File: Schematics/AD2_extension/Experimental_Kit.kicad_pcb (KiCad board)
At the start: 2 copper layers, 69.7 x 76.4 mm, 41 parts, among them J1 I2C, J10 AD2, J11 CN7, J12 CN10, J13 SPI_5V, J2 Keypad, J3 W2, J4 W1, J5 LCD, J6 SPI_3V3, J7 PWM, J8 PWM, J9 AREF, Q1 2N7002, Q2 2N7002, Q3 2N7002, Q4 2N7002, U1 TXU0304PW

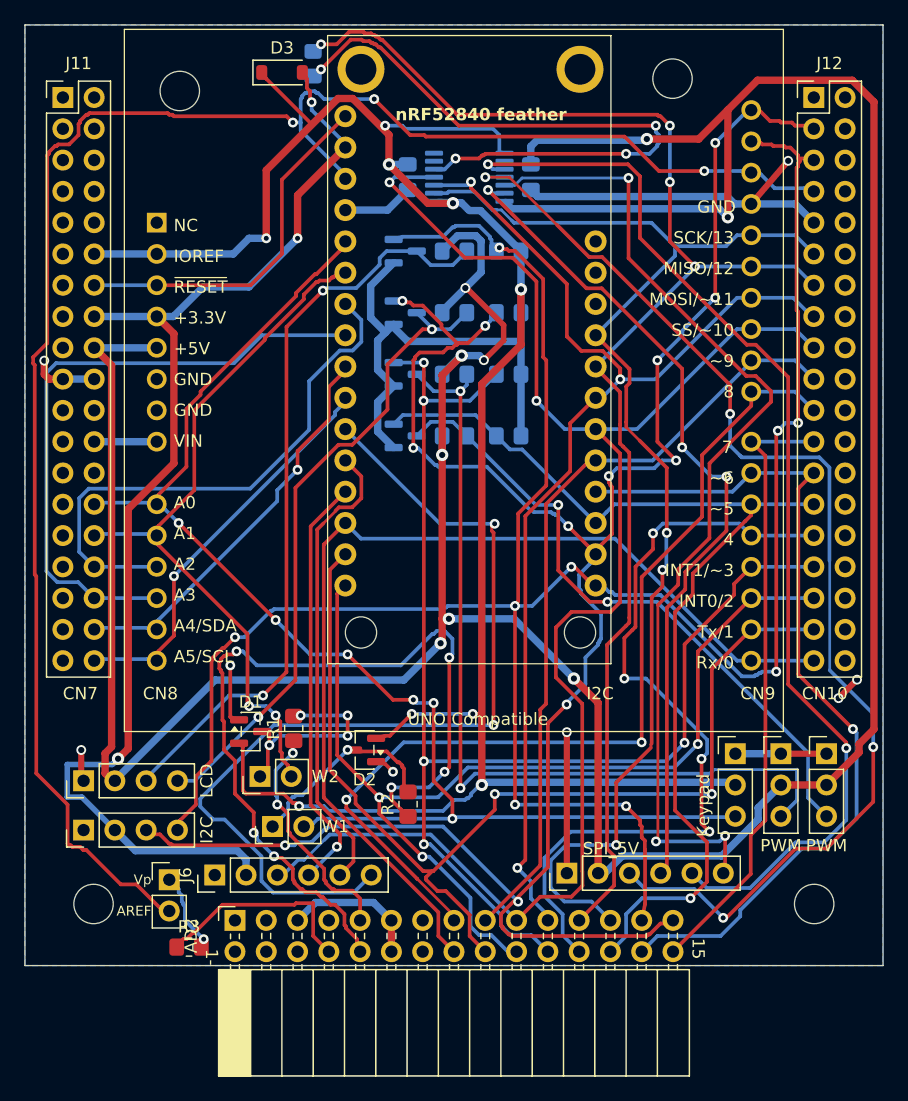
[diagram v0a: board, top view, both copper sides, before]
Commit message: AD2_extension: 보호회로·I2C 버스·Feather 5V 추가, DRC/ERC 무시 항목 0
회로도
- W1/W2 입력 보호: 직렬 1k + BAT54S 클램프, AD2 V+ -> AREF 직렬 4.7k
- IOREF 점퍼를 쇼트키 D3(+3V3 -> IOREF)로 교체
- LCD 시프터와 AD2 I2C를 UNO SDA/SCL, Nucleo PB9/PB8, Feather SDA/SCL 공용 버스로 이전
- U1(TXU0304) OE -> IOREF, MISO 직렬 R13 2.2k
- Feather USB -> D4 -> +5V
- J10/J11/J12 심볼을 필터를 맞춘 프로젝트 사본으로 교체

PCB
- 점퍼 재배치(Nucleo 외곽 밖), W1/W2 정렬, 신규 부품 배치·배선
- 상면 GND 붓기와 스티칭 비아 추가, 배선 직선/45도 정리
- 실크 정리, J10 기판 가장자리용 풋프린트, MS1 코트야드 면제
- ERC/DRC 위반 0, 무시 항목 0

Co-Authored-By: Claude Opus 5.5 <noreply@anthropic.com>
Claude-Session: https://claude.ai/code/session_0124difPG7KsZZNpLXnsU8d2
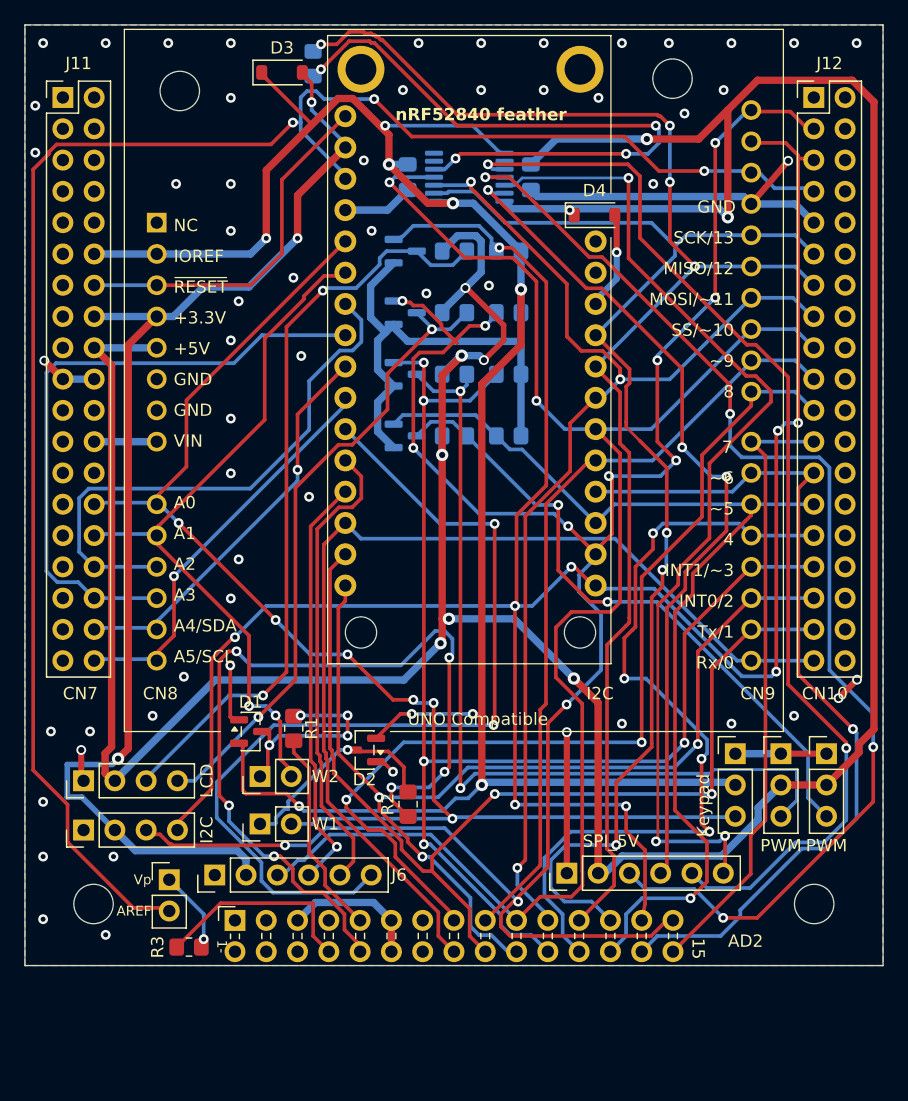
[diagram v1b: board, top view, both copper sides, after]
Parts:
- added D4: 1N5819HW, Diode_SMD:D_SOD-123, F.Cu at (123.2, 59.1)
- J10: footprint Connector_PinSocket_2.54mm:PinSocket_2x15_P2.54mm_Horizontal -> AD2_extension:PinSocket_2x15_P2.54mm_Horizontal_BoardEdge
- moved J4 1.04 mm to (96.0, 108.5)
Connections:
- MS1 pad 26: unconnected-(MS1-USB-Pad26) -> /FEATHER_USB
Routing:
- net /FEATHER_USB: track 0.00 -> 7.87 mm, vias 0 -> 1
- net /W2: track 18.9 -> 16.8 mm, vias 2 -> 0
- net Net-(J6-Pin_6): track 77.3 -> 75.5 mm
- net +3V3: track 99.3 -> 97.6 mm
- net AREF: track 144.1 -> 142.8 mm
- net Net-(D2-K1A2): track 15.9 -> 17.0 mm
- net /A0: track 106.9 -> 107.8 mm
- net /IOREF: track 211.4 -> 210.5 mm
- net /DIO1: track 85.0 -> 84.2 mm
- net GND: track 81.2 -> 80.5 mm, vias 8 -> 58
- net /DIO8: track 76.6 -> 77.3 mm
- net /A5: track 32.7 -> 32.2 mm
- net +5V: track 289.1 -> 289.0 mm, vias 9 -> 10
- added copper zone on F.Cu, net GND
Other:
- board text added: "Dept. of EEC, HKNU 26.10.30"
- board text removed: "Dept. of EEC, HKNU 26.10.09"

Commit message: AD2_extension: 회로도 정리 및 PCB 동기화, README에 이동 경로 추가
- 회로도 정리 반영, PCB 업데이트(FEATHER_USB 넷 → Net-(D4-A))
- ERC 0, DRC 0, 미연결 0, 회로도-PCB 패리티 0
- README: Schematics/AD2_extension 항목 추가(01_Lectures 저장소에서 이동)

Co-Authored-By: Claude Opus 5.5 <noreply@anthropic.com>
Claude-Session: https://claude.ai/code/session_0124difPG7KsZZNpLXnsU8d2
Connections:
- net /FEATHER_USB renamed Net-(D4-A)
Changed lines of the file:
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@@
 		(sheetname "/")
 		(sheetfile "Experimental_Kit.kicad_sch")
+		(units
+			(unit
+				(name "A")
+				(pins "1" "2")
+			)
+		)
 		(attr smd)
 		(duplicate_pad_numbers_are_jumpers no)
@@
 			(layers "F.Cu" "F.Mask" "F.Paste")
 			(roundrect_rratio 0.25)
-			(net "/FEATHER_USB")
+			(net "Net-(D4-A)")
 			(pinfunction "A_2")
 			(pintype "passive")
@@
 			)
 		)
-		(property ki_fp_filters "Connector*:*_2x??_*")
+		(property ki_fp_filters "PinSocket_2x19*Mirrored* Connector*:*_2x??_*")
 		(sheetname "/")
 		(sheetfile "Experimental_Kit.kicad_sch")
@@
 			)
 		)
-		(property ki_fp_filters "Connector*:*_2x??_*")
+		(property ki_fp_filters "PinSocket_2x19*Mirrored* Connector*:*_2x??_*")
 		(sheetname "/")
 		(sheetfile "Experimental_Kit.kicad_sch")
@@
 			(layers "*.Cu" "*.Mask")
 			(remove_unused_layers no)
-			(net "/FEATHER_USB")
+			(net "Net-(D4-A)")
 			(pinfunction "USB_26")
-			(pintype "power_in+no_connect")
+			(pintype "power_in")
 			(solder_mask_margin 0.0508)
 			(thermal_bridge_angle 0)
@@
 			)
 		)
-		(property ki_fp_filters "Connector*:*_2x??_*")
+		(property ki_fp_filters "PinSocket_2x15*BoardEdge* Connector*:*_2x??_*")
 		(sheetname "/")
 		(sheetfile "Experimental_Kit.kicad_sch")
@@
 		(sheetname "/")
 		(sheetfile "Experimental_Kit.kicad_sch")
+		(units
+			(unit
+				(name "A")
+				(pins "1" "2")
+			)
+		)
 		(attr smd)
 		(duplicate_pad_numbers_are_jumpers no)
@@
 	)
 	(segment
-		(start 124.968 62.103)
-		(end 124.968 59.563)
-		(width 0.5)
-		(layer "F.Cu")
-		(net "/FEATHER_USB")
-	)
-	(segment
-		(start 124.968 59.563)
-		(end 124.815999 59.084)
-		(width 0.5)
-		(layer "F.Cu")
-		(net "/FEATHER_USB")
-	)
-	(via
-		(at 124.968 62.103)
-		(size 0.8)
-		(drill 0.4)
-		(layers "F.Cu" "B.Cu")
-		(net "/FEATHER_USB")
-	)
-	(segment
-		(start 123.698 65.532)
-		(end 124.968 64.261999)
-		(width 0.5)
-		(layer "B.Cu")
-		(net "/FEATHER_USB")
-	)
-	(segment
-		(start 124.968 64.261999)
-		(end 124.968 62.103)
-		(width 0.5)
-		(layer "B.Cu")
-		(net "/FEATHER_USB")
-	)
-	(segment
-		(start 123.26 66.29)
-		(end 123.698 65.532)
-		(width 0.5)
-		(layer "B.Cu")
-		(net "/FEATHER_USB")
-	)
-	(segment
 		(start 87.884 109.347)
 		(end 88.646 110.109)
@@
 		(net "/MISO_IO")
 	)
+	(segment
+		(start 124.968 62.103)
+		(end 124.968 59.563)
+		(width 0.5)
+		(layer "F.Cu")
+		(net "Net-(D4-A)")
+	)
+	(segment
+		(start 124.968 59.563)
+		(end 124.815999 59.084)
+		(width 0.5)
+		(layer "F.Cu")
+		(net "Net-(D4-A)")
+	)
+	(via
+		(at 124.968 62.103)
+		(size 0.8)
+		(drill 0.4)
+		(layers "F.Cu" "B.Cu")
+		(net "Net-(D4-A)")
+	)
+	(segment
+		(start 123.698 65.532)
+		(end 124.968 64.261999)
+		(width 0.5)
+		(layer "B.Cu")
+		(net "Net-(D4-A)")
+	)
+	(segment
+		(start 124.968 64.261999)
+		(end 124.968 62.103)
+		(width 0.5)
+		(layer "B.Cu")
+		(net "Net-(D4-A)")
+	)
+	(segment
+		(start 123.26 66.29)
+		(end 123.698 65.532)
+		(width 0.5)
+		(layer "B.Cu")
+		(net "Net-(D4-A)")
+	)
 	(zone
